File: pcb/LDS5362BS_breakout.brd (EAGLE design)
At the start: 100 x 80 mm, 11 parts

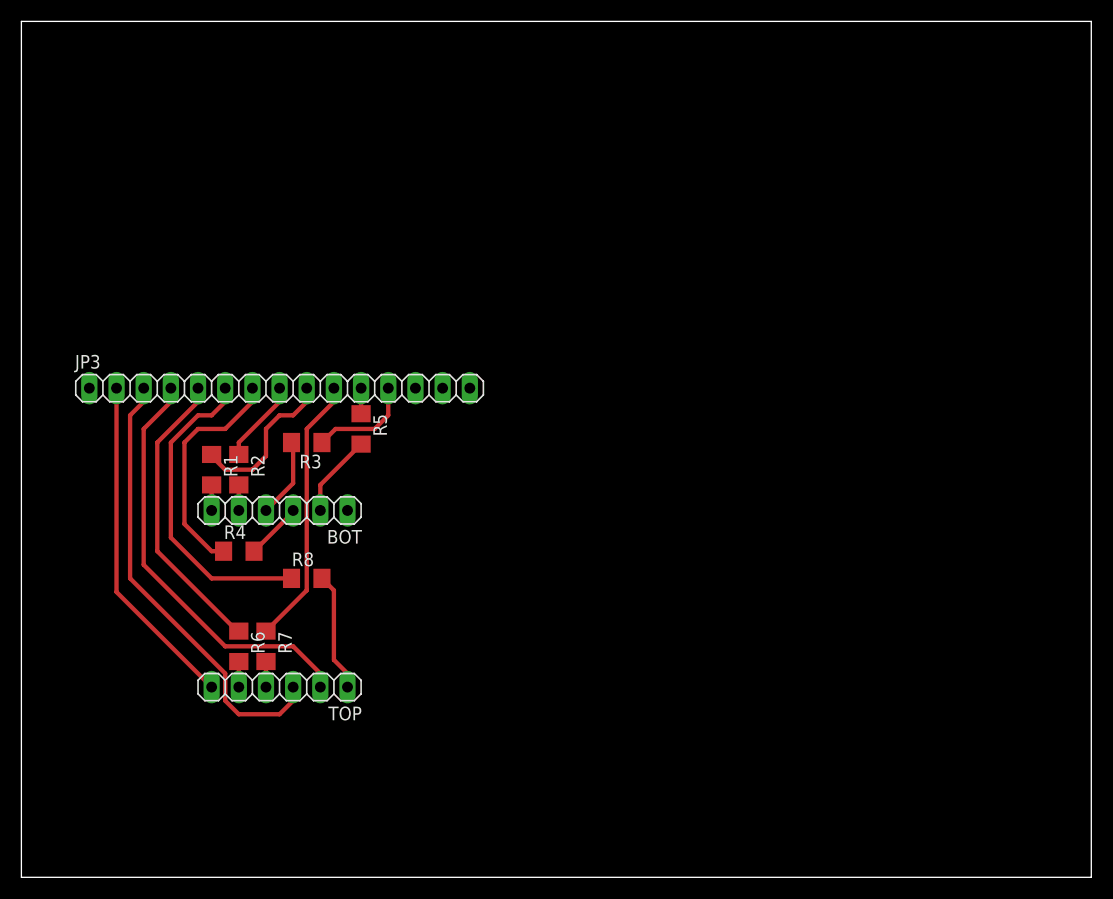
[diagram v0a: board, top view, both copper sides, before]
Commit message: Fixed board dimentions & added GND plane.
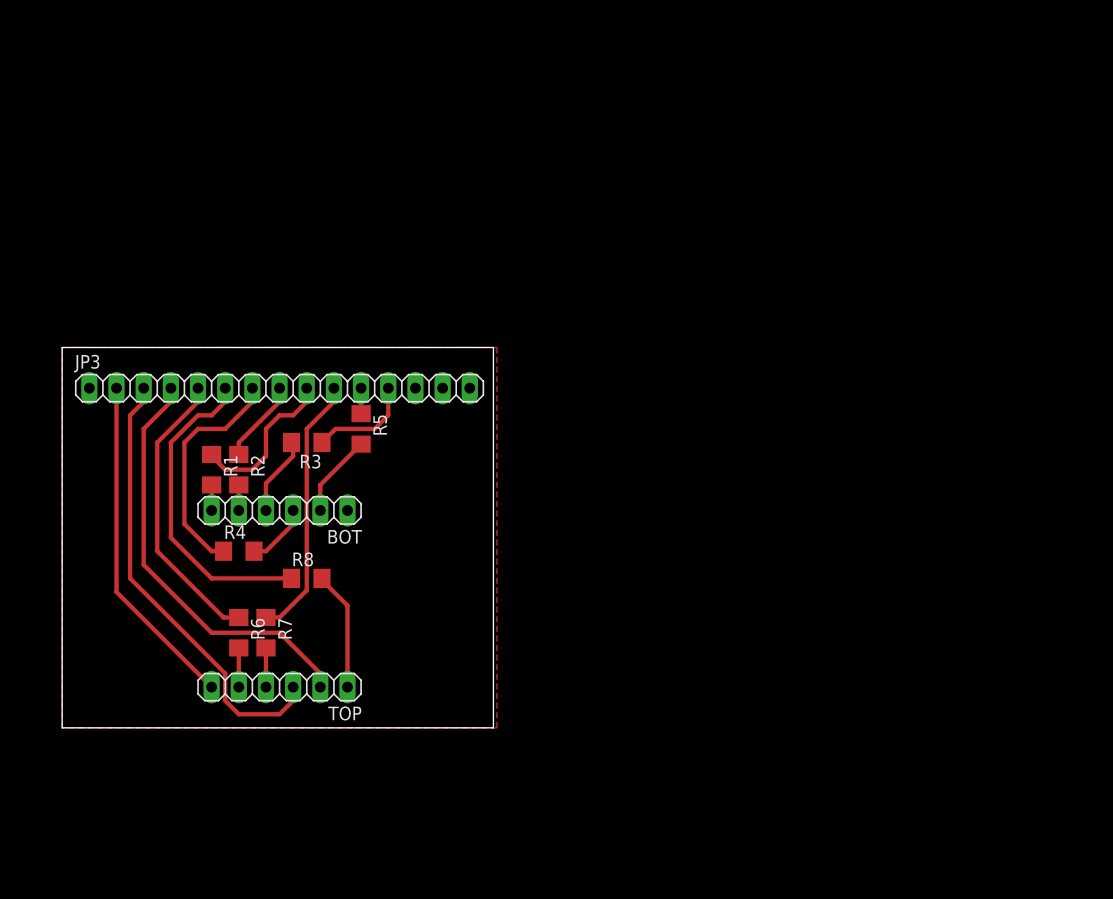
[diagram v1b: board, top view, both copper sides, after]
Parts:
- moved R6 1.27 mm to (20.3, 22.9)
- moved R7 1.27 mm to (22.9, 22.9)
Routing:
- net N$3: track 2.39 -> 3.66 mm
- net N$2: track 2.39 -> 3.66 mm
- net N$1: track 11.1 -> 12.4 mm
- net N$5: track 5.33 -> 5.98 mm
- net F: track 25.3 -> 24.8 mm
- net A: track 27.5 -> 27.0 mm
- added copper zone on layer 1, net GND
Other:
- board size 100 x 80 mm -> 40.3 x 35.6 mm
